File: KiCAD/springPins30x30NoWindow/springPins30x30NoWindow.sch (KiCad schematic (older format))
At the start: 24 parts, among them J1 CONN_01X03, J2 CONN_01X03, J3 CONN_01X03, J4 CONN_01X03, J5 CONN_01X03, J6 CONN_01X03, J7 CONN_01X03, J8 CONN_01X03

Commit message: nowindow pin boards done
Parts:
- removed J1, J2, J3, J4, J5, J6, J7, J8: CONN_01X03, myParts:M50-3130342, symbol CONN_01X03
- added J1, J2: CONN_02X06, Pin_Headers:Pin_Header_Straight_2x06_Pitch2.54mm, symbol CONN_02X06
- added R1: 200k, Resistors_SMD:R_0805_HandSoldering, symbol R
- renumbered TP2 to TP10, TP16 to TP11, TP1 to TP12, TP14 to TP15, TP12 to TP16, TP10 to TP17, TP8 to TP18, TP6 to TP19, TP4 to TP20, TP13 to TP3, TP11 to TP4, TP9 to TP5, TP7 to TP6, TP5 to TP7, TP3 to TP8, TP15 to TP9
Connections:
- net labels added: BCu, FCu, I1, I2, I3, I4, I5, I6, IB, IT, RH, RL, V1, V2, V3, V4, V5, V6, VB, VT
- net labels removed: +3.3V, +5V, 0_I, 0_V, 1_I, 1_V, 2_I, 2_V, 3_I, 3_V, 4_I, 4_V, 5_I, 5_V, GND, L_I, L_V, MISO, MOSI, R_I, R_V, SCK, SCL, SDA
- wire segments 11 -> 50
- no-connect marks 5 -> 6
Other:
- note added: "+"
- note added: "1"
- note added: "2"
- note added: "3"
- note added: "4"
- note added: "5"
- note added: "6"
- note added: "Board Type\nEncoding Resistor"
- note added: "o"
- moved on the sheet: TP10, TP11, TP12, TP15, TP16, TP17, TP18, TP19, TP20, TP3, TP4, TP5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

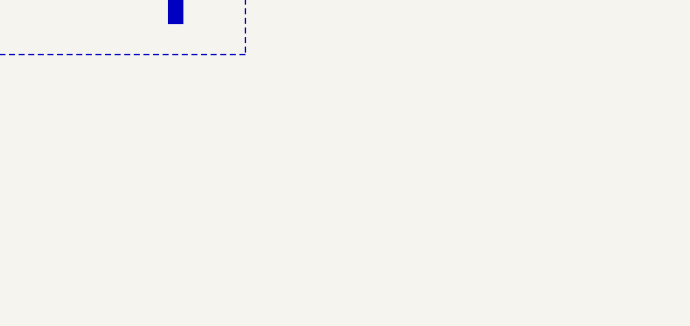
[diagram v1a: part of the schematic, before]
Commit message: 30x30NoWindow spruce up
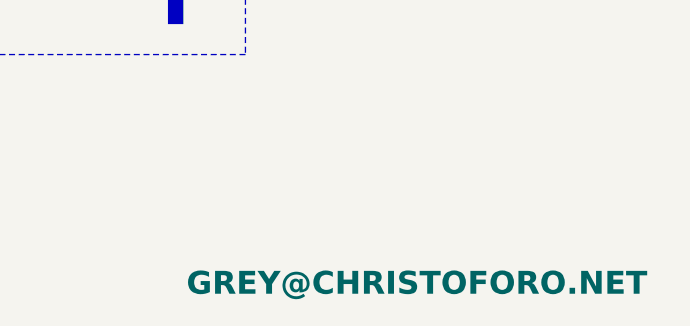
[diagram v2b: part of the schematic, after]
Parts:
- added L1: GREY@CHRISTOFORO.NET, myParts:logo_small, symbol GREY@CHRISTOFORO.NET
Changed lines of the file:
@@
 EESchema Schematic File Version 2
+LIBS:myParts
 LIBS:power
 LIBS:device
@@
 NoConn ~ 5500 3750
 NoConn ~ 4850 3750
+$Comp
+L GREY@CHRISTOFORO.NET L1
+U 1 1 59BFB10C
+P 7950 6950
+F 0 "L1" H 7950 6825 60  0001 C CNN
+F 1 "GREY@CHRISTOFORO.NET" H 7950 6950 100 0000 C CNB
+F 2 "myParts:logo_small" H 7950 6950 60  0001 C CNN
+F 3 "" H 7950 6950 60  0001 C CNN
+	1    7950 6950
+	1    0    0    -1
+$EndComp
 $EndSCHEMATC

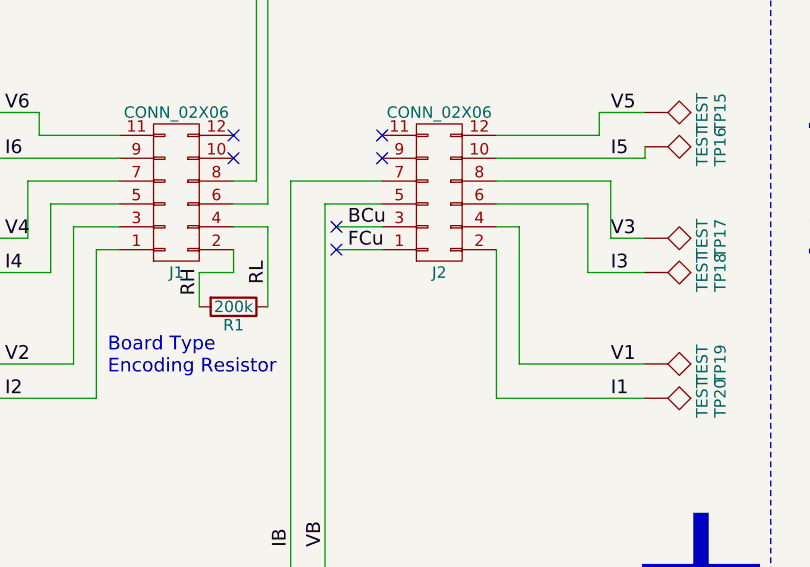
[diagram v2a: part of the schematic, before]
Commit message: make spring pin board pin holders smaller, update base1x, update mux design controller board
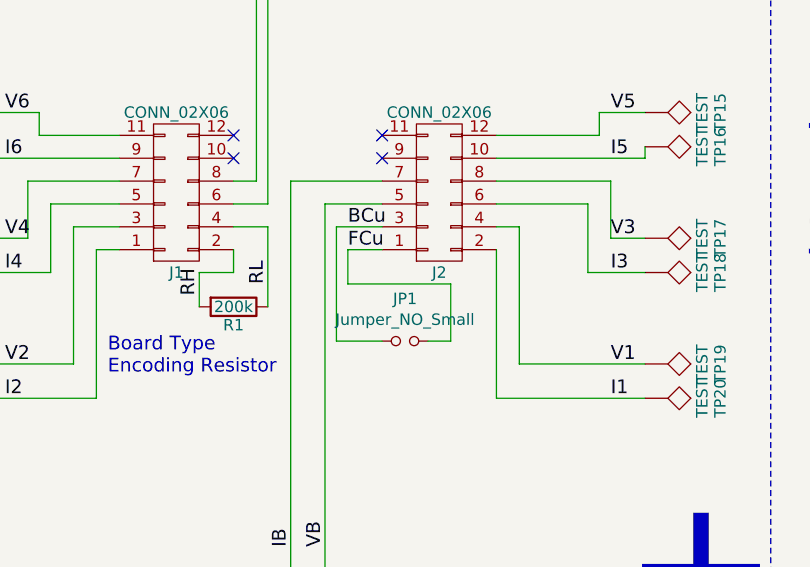
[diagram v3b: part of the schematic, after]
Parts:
- added JP1: Jumper_NO_Small, Connectors:GS2, symbol Jumper_NO_Small
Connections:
- net BCu: now also JP1.1
- net FCu: now also JP1.2
- no-connect marks 6 -> 4
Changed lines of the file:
@@
 LIBS:valves
 LIBS:springPins30x30NoWindow-cache
-EELAYER 25 0
+EELAYER 26 0
 EELAYER END
 $Descr A4 11693 8268
@@
 RH
 Wire Wire Line
-	5300 4150 5500 4150
+	5350 4150 5500 4150
 Wire Wire Line
 	5500 4050 5300 4050
-NoConn ~ 5300 4150
-NoConn ~ 5300 4050
 Text Label 5350 4150 0    60   ~ 0
 FCu
@@
 	1    0    0    -1
 $EndComp
+$Comp
+L Jumper_NO_Small JP1
+U 1 1 59F4B423
+P 5600 4550
+F 0 "JP1" H 5600 4735 50  0000 C CNN
+F 1 "Jumper_NO_Small" H 5600 4644 50  0000 C CNN
+F 2 "Connectors:GS2" H 5600 4550 50  0001 C CNN
+F 3 "" H 5600 4550 50  0001 C CNN
+	1    5600 4550
+	1    0    0    -1
+$EndComp
+Wire Wire Line
+	5300 4050 5300 4550
+Wire Wire Line
+	5300 4550 5500 4550
+Wire Wire Line
+	5350 4150 5350 4300
+Wire Wire Line
+	5350 4300 5800 4300
+Wire Wire Line
+	5800 4300 5800 4550
+Wire Wire Line
+	5800 4550 5700 4550
 $EndSCHEMATC

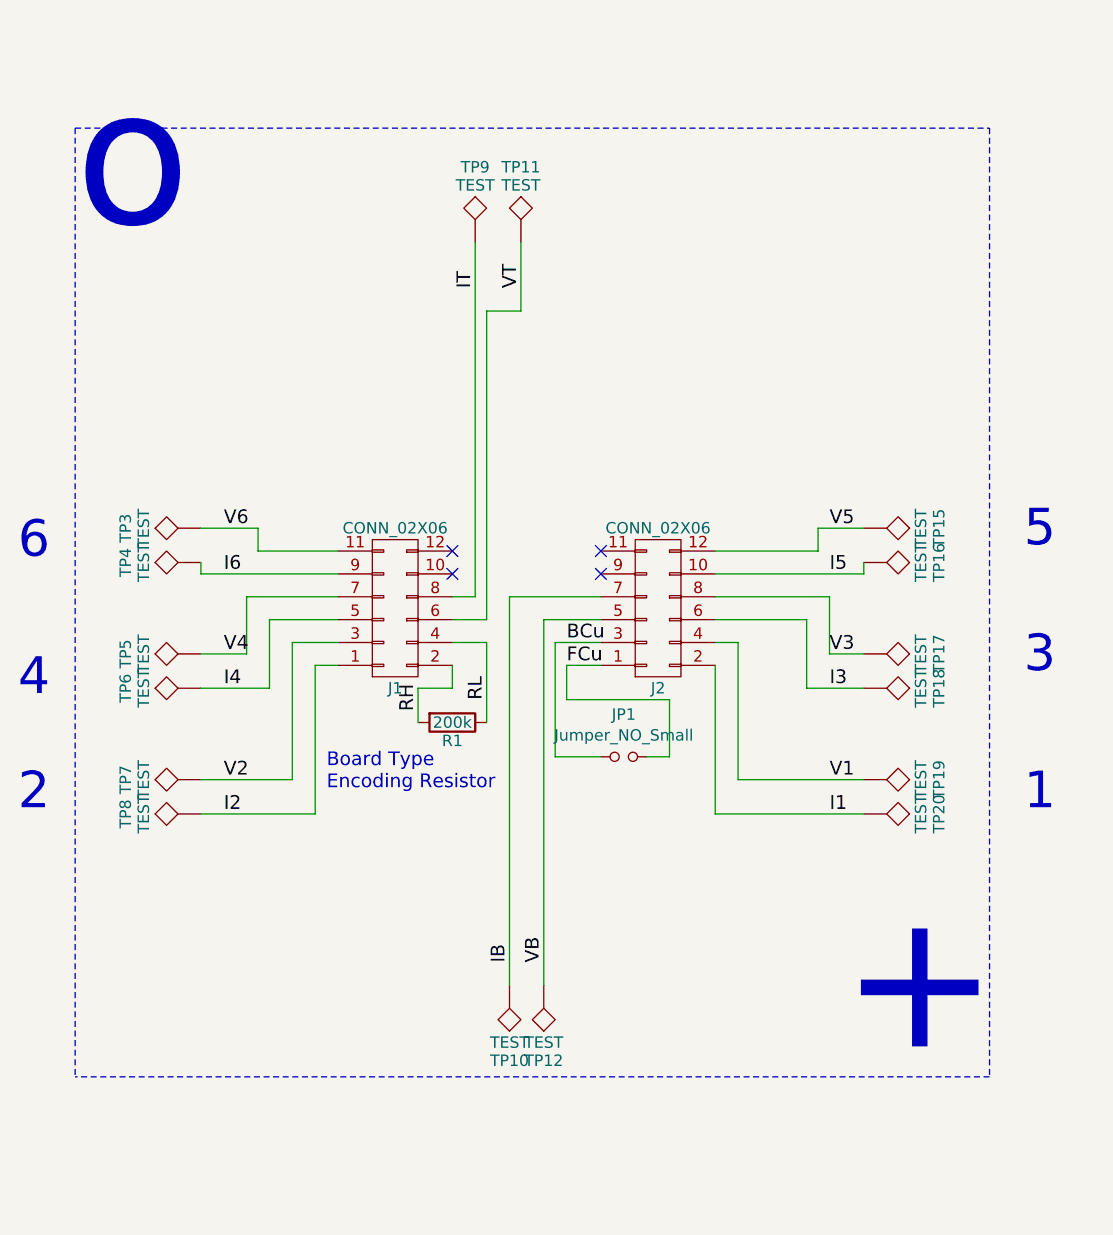
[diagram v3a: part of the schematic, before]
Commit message: rotate connectors on newMux
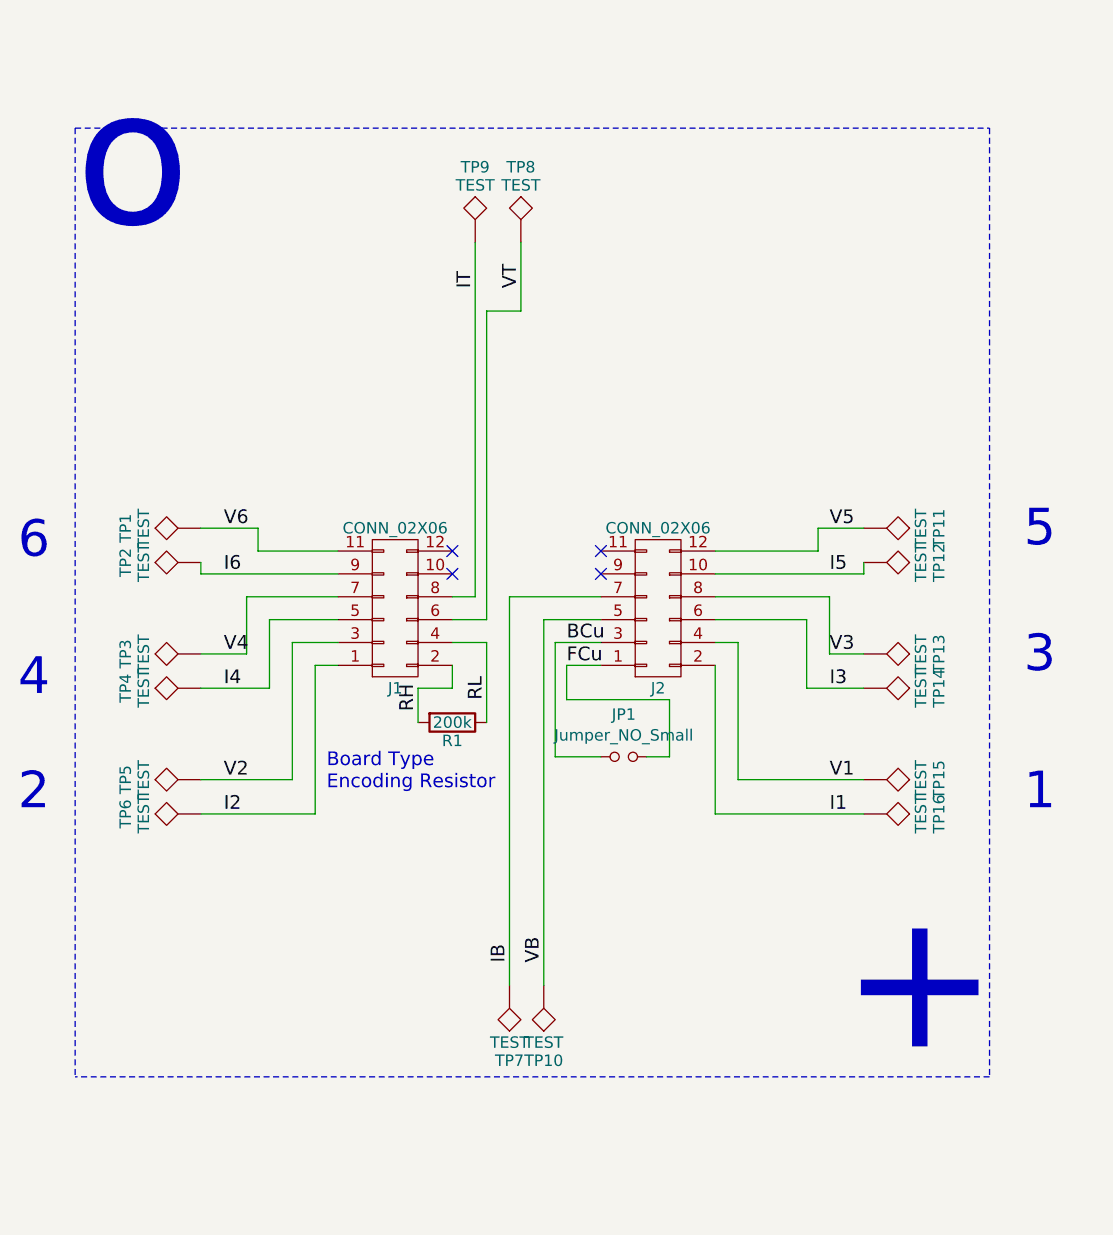
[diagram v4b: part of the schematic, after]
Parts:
- removed TP17, TP18, TP19, TP20: TEST, myParts:S25-022+P25-4023, symbol TEST
- added TP1, TP13, TP14, TP2: TEST, myParts:S25-022+P25-4023, symbol TEST
- TP10, TP11, TP12, TP15, TP16, TP3, TP4, TP5, TP6, TP7, TP8, TP9: farnellCode (none) -> 9960260 + 9960244
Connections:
- net I1: now also TP16.1
- net I2: now also TP6.1; no longer TP8.1
- net I3: now also TP14.1
- net I4: now also TP4.1; no longer TP6.1
- net I5: now also TP12.1; no longer TP16.1
- net I6: now also TP2.1; no longer TP4.1
- net IB: now also TP7.1; no longer TP10.1
- net V1: now also TP15.1
- net V2: now also TP5.1; no longer TP7.1
- net V3: now also TP13.1
- net V4: now also TP3.1; no longer TP5.1
- net V5: now also TP11.1; no longer TP15.1
- net V6: now also TP1.1; no longer TP3.1
- net VB: now also TP10.1; no longer TP12.1
- net VT: now also TP8.1; no longer TP11.1
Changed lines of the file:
@@
 LIBS:power
 LIBS:device
-LIBS:transistors
-LIBS:conn
 LIBS:linear
 LIBS:regul
-LIBS:74xx
-LIBS:cmos4000
 LIBS:adc-dac
 LIBS:memory
@@
 LIBS:digital-audio
 LIBS:philips
-LIBS:display
 LIBS:cypress
 LIBS:siliconi
@@
 LIBS:atmel
 LIBS:contrib
-LIBS:valves
 LIBS:springPins30x30NoWindow-cache
 EELAYER 26 0
@@
 $EndDescr
 $Comp
-L TEST TP10
-U 1 1 58E4C4C8
-P 5100 5550
-F 0 "TP10" H 5100 5850 50  0000 C BNN
-F 1 "TEST" H 5100 5800 50  0000 C CNN
-F 2 "myParts:S25-022+P25-4023" H 5100 5550 50  0001 C CNN
-F 3 "" H 5100 5550 50  0000 C CNN
-	1    5100 5550
-	-1   0    0    1
-$EndComp
-$Comp
-L TEST TP6
-U 1 1 58E4C4F2
-P 3750 4250
-F 0 "TP6" H 3750 4550 50  0000 C BNN
-F 1 "TEST" H 3750 4500 50  0000 C CNN
-F 2 "myParts:S25-022+P25-4023" H 3750 4250 50  0001 C CNN
-F 3 "" H 3750 4250 50  0000 C CNN
-	1    3750 4250
-	0    -1   -1   0
-$EndComp
-$Comp
-L TEST TP5
-U 1 1 58E4C553
-P 3750 4100
-F 0 "TP5" H 3750 4400 50  0000 C BNN
-F 1 "TEST" H 3750 4350 50  0000 C CNN
-F 2 "myParts:S25-022+P25-4023" H 3750 4100 50  0001 C CNN
-F 3 "" H 3750 4100 50  0000 C CNN
-	1    3750 4100
-	0    -1   -1   0
-$EndComp
-$Comp
-L TEST TP8
-U 1 1 58E4C6B7
-P 3750 4800
-F 0 "TP8" H 3750 5100 50  0000 C BNN
-F 1 "TEST" H 3750 5050 50  0000 C CNN
-F 2 "myParts:S25-022+P25-4023" H 3750 4800 50  0001 C CNN
-F 3 "" H 3750 4800 50  0000 C CNN
-	1    3750 4800
-	0    -1   -1   0
-$EndComp
-$Comp
-L TEST TP7
-U 1 1 58E4C6BD
-P 3750 4650
-F 0 "TP7" H 3750 4950 50  0000 C BNN
-F 1 "TEST" H 3750 4900 50  0000 C CNN
-F 2 "myParts:S25-022+P25-4023" H 3750 4650 50  0001 C CNN
-F 3 "" H 3750 4650 50  0000 C CNN
-	1    3750 4650
-	0    -1   -1   0
-$EndComp
-$Comp
-L TEST TP4
-U 1 1 58E4C747
-P 3750 3700
-F 0 "TP4" H 3750 4000 50  0000 C BNN
-F 1 "TEST" H 3750 3950 50  0000 C CNN
-F 2 "myParts:S25-022+P25-4023" H 3750 3700 50  0001 C CNN
-F 3 "" H 3750 3700 50  0000 C CNN
-	1    3750 3700
-	0    -1   -1   0
-$EndComp
-$Comp
-L TEST TP3
-U 1 1 58E4C74D
-P 3750 3550
-F 0 "TP3" H 3750 3850 50  0000 C BNN
-F 1 "TEST" H 3750 3800 50  0000 C CNN
-F 2 "myParts:S25-022+P25-4023" H 3750 3550 50  0001 C CNN
-F 3 "" H 3750 3550 50  0000 C CNN
-	1    3750 3550
-	0    -1   -1   0
-$EndComp
-$Comp
-L TEST TP18
-U 1 1 58E4CA5F
-P 6650 4250
-F 0 "TP18" H 6650 4550 50  0000 C BNN
-F 1 "TEST" H 6650 4500 50  0000 C CNN
-F 2 "myParts:S25-022+P25-4023" H 6650 4250 50  0001 C CNN
-F 3 "" H 6650 4250 50  0000 C CNN
-	1    6650 4250
-	0    1    -1   0
-$EndComp
-$Comp
-L TEST TP17
-U 1 1 58E4CA65
-P 6650 4100
-F 0 "TP17" H 6650 4400 50  0000 C BNN
-F 1 "TEST" H 6650 4350 50  0000 C CNN
-F 2 "myParts:S25-022+P25-4023" H 6650 4100 50  0001 C CNN
-F 3 "" H 6650 4100 50  0000 C CNN
-	1    6650 4100
-	0    1    -1   0
-$EndComp
-$Comp
-L TEST TP20
-U 1 1 58E4CA6B
-P 6650 4800
-F 0 "TP20" H 6650 5100 50  0000 C BNN
-F 1 "TEST" H 6650 5050 50  0000 C CNN
-F 2 "myParts:S25-022+P25-4023" H 6650 4800 50  0001 C CNN
-F 3 "" H 6650 4800 50  0000 C CNN
-	1    6650 4800
-	0    1    -1   0
-$EndComp
-$Comp
-L TEST TP19
-U 1 1 58E4CA71
-P 6650 4650
-F 0 "TP19" H 6650 4950 50  0000 C BNN
-F 1 "TEST" H 6650 4900 50  0000 C CNN
-F 2 "myParts:S25-022+P25-4023" H 6650 4650 50  0001 C CNN
-F 3 "" H 6650 4650 50  0000 C CNN
-	1    6650 4650
-	0    1    -1   0
-$EndComp
-$Comp
-L TEST TP16
-U 1 1 58E4CA77
-P 6650 3700
-F 0 "TP16" H 6650 4000 50  0000 C BNN
-F 1 "TEST" H 6650 3950 50  0000 C CNN
-F 2 "myParts:S25-022+P25-4023" H 6650 3700 50  0001 C CNN
-F 3 "" H 6650 3700 50  0000 C CNN
-	1    6650 3700
-	0    1    -1   0
-$EndComp
-$Comp
-L TEST TP15
-U 1 1 58E4CA7D
-P 6650 3550
-F 0 "TP15" H 6650 3850 50  0000 C BNN
-F 1 "TEST" H 6650 3800 50  0000 C CNN
-F 2 "myParts:S25-022+P25-4023" H 6650 3550 50  0001 C CNN
-F 3 "" H 6650 3550 50  0000 C CNN
-	1    6650 3550
-	0    1    -1   0
-$EndComp
-$Comp
 L TEST TP9
 U 1 1 58E4CC43
@@
 F 2 "myParts:S25-022+P25-4023" H 4950 2300 50  0001 C CNN
 F 3 "" H 4950 2300 50  0000 C CNN
+F 4 "9960260 + 9960244" H 4950 2300 60  0001 C CNN "farnellCode"
 	1    4950 2300
-	-1   0    0    -1
-$EndComp
-$Comp
-L TEST TP11
-U 1 1 58E4CC49
-P 5150 2300
-F 0 "TP11" H 5150 2600 50  0000 C BNN
-F 1 "TEST" H 5150 2550 50  0000 C CNN
-F 2 "myParts:S25-022+P25-4023" H 5150 2300 50  0001 C CNN
-F 3 "" H 5150 2300 50  0000 C CNN
-	1    5150 2300
 	-1   0    0    -1
 $EndComp
@@
 Wire Wire Line
 	4000 3550 3750 3550
-$Comp
-L TEST TP12
-U 1 1 58E4C3ED
-P 5250 5550
-F 0 "TP12" H 5250 5850 50  0000 C BNN
-F 1 "TEST" H 5250 5800 50  0000 C CNN
-F 2 "myParts:S25-022+P25-4023" H 5250 5550 50  0001 C CNN
-F 3 "" H 5250 5550 50  0000 C CNN
-	1    5250 5550
-	-1   0    0    1
-$EndComp
 Wire Wire Line
 	4950 2300 4950 3850
@@
 Wire Wire Line
 	5800 4550 5700 4550
+$Comp
+L TEST TP8
+U 1 1 5A65C96D
+P 5150 2300
+F 0 "TP8" H 5150 2600 50  0000 C BNN
+F 1 "TEST" H 5150 2550 50  0000 C CNN
+F 2 "myParts:S25-022+P25-4023" H 5150 2300 50  0001 C CNN
+F 3 "" H 5150 2300 50  0000 C CNN
+F 4 "9960260 + 9960244" H 5150 2300 60  0001 C CNN "farnellCode"
+	1    5150 2300
+	-1   0    0    -1
+$EndComp
+$Comp
+L TEST TP11
+U 1 1 5A65C9A7
+P 6650 3550
+F 0 "TP11" H 6650 3850 50  0000 C BNN
+F 1 "TEST" H 6650 3800 50  0000 C CNN
+F 2 "myParts:S25-022+P25-4023" H 6650 3550 50  0001 C CNN
+F 3 "" H 6650 3550 50  0000 C CNN
+F 4 "9960260 + 9960244" H 6650 3550 60  0001 C CNN "farnellCode"
+	1    6650 3550
+	0    1    -1   0
+$EndComp
+$Comp
+L TEST TP12
+U 1 1 5A65CA0A
+P 6650 3700
+F 0 "TP12" H 6650 4000 50  0000 C BNN
+F 1 "TEST" H 6650 3950 50  0000 C CNN
+F 2 "myParts:S25-022+P25-4023" H 6650 3700 50  0001 C CNN
+F 3 "" H 6650 3700 50  0000 C CNN
+F 4 "9960260 + 9960244" H 6650 3700 60  0001 C CNN "farnellCode"
+	1    6650 3700
+	0    1    -1   0
+$EndComp
+$Comp
+L TEST TP13
+U 1 1 5A65CA32
+P 6650 4100
+F 0 "TP13" H 6650 4400 50  0000 C BNN
+F 1 "TEST" H 6650 4350 50  0000 C CNN
+F 2 "myParts:S25-022+P25-4023" H 6650 4100 50  0001 C CNN
+F 3 "" H 6650 4100 50  0000 C CNN
+F 4 "9960260 + 9960244" H 6650 4100 60  0001 C CNN "farnellCode"
+	1    6650 4100
+	0    1    -1   0
+$EndComp
+$Comp
+L TEST TP14
+U 1 1 5A65CA62
+P 6650 4250
+F 0 "TP14" H 6650 4550 50  0000 C BNN
+F 1 "TEST" H 6650 4500 50  0000 C CNN
+F 2 "myParts:S25-022+P25-4023" H 6650 4250 50  0001 C CNN
+F 3 "" H 6650 4250 50  0000 C CNN
+F 4 "9960260 + 9960244" H 6650 4250 60  0001 C CNN "farnellCode"
+	1    6650 4250
+	0    1    -1   0
+$EndComp
+$Comp
+L TEST TP15
+U 1 1 5A65CA8E
+P 6650 4650
+F 0 "TP15" H 6650 4950 50  0000 C BNN
+F 1 "TEST" H 6650 4900 50  0000 C CNN
+F 2 "myParts:S25-022+P25-4023" H 6650 4650 50  0001 C CNN
+F 3 "" H 6650 4650 50  0000 C CNN
+F 4 "9960260 + 9960244" H 6650 4650 60  0001 C CNN "farnellCode"
+	1    6650 4650
+	0    1    -1   0
+$EndComp
+$Comp
+L TEST TP16
+U 1 1 5A65CAC6
+P 6650 4800
+F 0 "TP16" H 6650 5100 50  0000 C BNN
+F 1 "TEST" H 6650 5050 50  0000 C CNN
+F 2 "myParts:S25-022+P25-4023" H 6650 4800 50  0001 C CNN
+F 3 "" H 6650 4800 50  0000 C CNN
+F 4 "9960260 + 9960244" H 6650 4800 60  0001 C CNN "farnellCode"
+	1    6650 4800
+	0    1    -1   0
+$EndComp
+$Comp
+L TEST TP10
+U 1 1 5A65CAF2
+P 5250 5550
+F 0 "TP10" H 5250 5850 50  0000 C BNN
+F 1 "TEST" H 5250 5800 50  0000 C CNN
+F 2 "myParts:S25-022+P25-4023" H 5250 5550 50  0001 C CNN
+F 3 "" H 5250 5550 50  0000 C CNN
+F 4 "9960260 + 9960244" H 5250 5550 60  0001 C CNN "farnellCode"
+	1    5250 5550
+	1    0    0    1
+$EndComp
+$Comp
+L TEST TP7
+U 1 1 5A65CB55
+P 5100 5550
+F 0 "TP7" H 5100 5850 50  0000 C BNN
+F 1 "TEST" H 5100 5800 50  0000 C CNN
+F 2 "myParts:S25-022+P25-4023" H 5100 5550 50  0001 C CNN
+F 3 "" H 5100 5550 50  0000 C CNN
+F 4 "9960260 + 9960244" H 5100 5550 60  0001 C CNN "farnellCode"
+	1    5100 5550
+	1    0    0    1
+$EndComp
+$Comp
+L TEST TP6
+U 1 1 5A65CC03
+P 3750 4800
+F 0 "TP6" H 3750 5100 50  0000 C BNN
+F 1 "TEST" H 3750 5050 50  0000 C CNN
+F 2 "myParts:S25-022+P25-4023" H 3750 4800 50  0001 C CNN
+F 3 "" H 3750 4800 50  0000 C CNN
+F 4 "9960260 + 9960244" H 3750 4800 60  0001 C CNN "farnellCode"
+	1    3750 4800
+	0    -1   1    0
+$EndComp
+$Comp
+L TEST TP5
+U 1 1 5A65CC8C
+P 3750 4650
+F 0 "TP5" H 3750 4950 50  0000 C BNN
+F 1 "TEST" H 3750 4900 50  0000 C CNN
+F 2 "myParts:S25-022+P25-4023" H 3750 4650 50  0001 C CNN
+F 3 "" H 3750 4650 50  0000 C CNN
+F 4 "9960260 + 9960244" H 3750 4650 60  0001 C CNN "farnellCode"
+	1    3750 4650
+	0    -1   1    0
+$EndComp
+$Comp
+L TEST TP4
+U 1 1 5A65CCC0
+P 3750 4250
+F 0 "TP4" H 3750 4550 50  0000 C BNN
+F 1 "TEST" H 3750 4500 50  0000 C CNN
+F 2 "myParts:S25-022+P25-4023" H 3750 4250 50  0001 C CNN
+F 3 "" H 3750 4250 50  0000 C CNN
+F 4 "9960260 + 9960244" H 3750 4250 60  0001 C CNN "farnellCode"
+	1    3750 4250
+	0    -1   1    0
+$EndComp
+$Comp
+L TEST TP3
+U 1 1 5A65CCFE
+P 3750 4100
+F 0 "TP3" H 3750 4400 50  0000 C BNN
+F 1 "TEST" H 3750 4350 50  0000 C CNN
+F 2 "myParts:S25-022+P25-4023" H 3750 4100 50  0001 C CNN
+F 3 "" H 3750 4100 50  0000 C CNN
+F 4 "9960260 + 9960244" H 3750 4100 60  0001 C CNN "farnellCode"
+	1    3750 4100
+	0    -1   1    0
+$EndComp
+$Comp
+L TEST TP2
+U 1 1 5A65CD36
+P 3750 3700
+F 0 "TP2" H 3750 4000 50  0000 C BNN
+F 1 "TEST" H 3750 3950 50  0000 C CNN
+F 2 "myParts:S25-022+P25-4023" H 3750 3700 50  0001 C CNN
+F 3 "" H 3750 3700 50  0000 C CNN
+F 4 "9960260 + 9960244" H 3750 3700 60  0001 C CNN "farnellCode"
+	1    3750 3700
+	0    -1   1    0
+$EndComp
+$Comp
+L TEST TP1
+U 1 1 5A65CD7A
+P 3750 3550
+F 0 "TP1" H 3750 3850 50  0000 C BNN
+F 1 "TEST" H 3750 3800 50  0000 C CNN
+F 2 "myParts:S25-022+P25-4023" H 3750 3550 50  0001 C CNN
+F 3 "" H 3750 3550 50  0000 C CNN
+F 4 "9960260 + 9960244" H 3750 3550 60  0001 C CNN "farnellCode"
+	1    3750 3550
+	0    -1   1    0
+$EndComp
 $EndSCHEMATC
